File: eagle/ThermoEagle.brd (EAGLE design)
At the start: 100 x 80 mm, 30 parts, among them IC1 MAX232, IC2 4511N, Q1 20MHz, T1 2N2219, T2 2N2219, U1 LM324

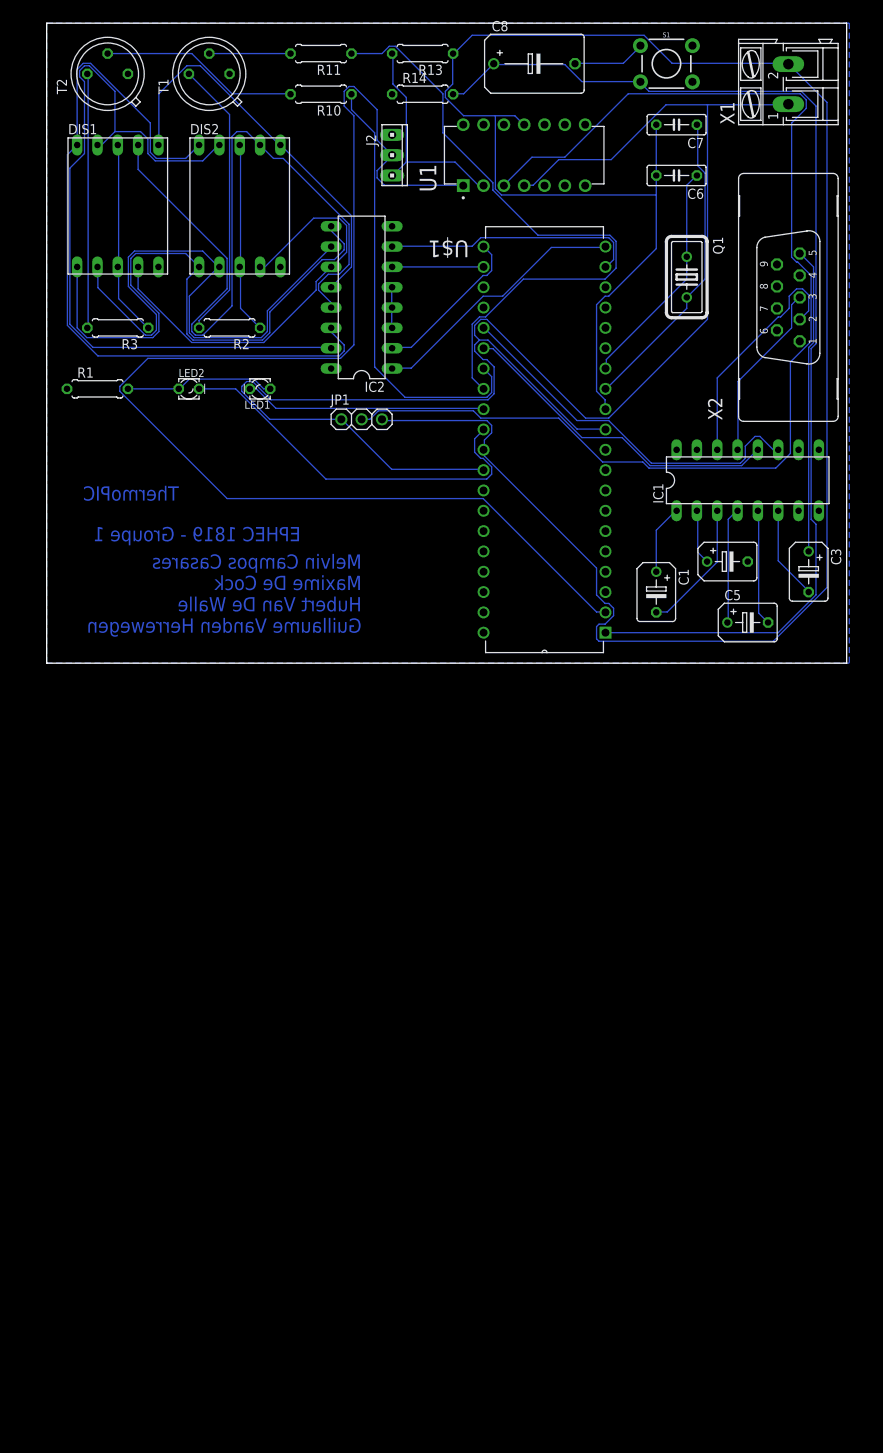
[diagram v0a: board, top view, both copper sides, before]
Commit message: connector
ajout des connecteurs, pour les parties non connectées
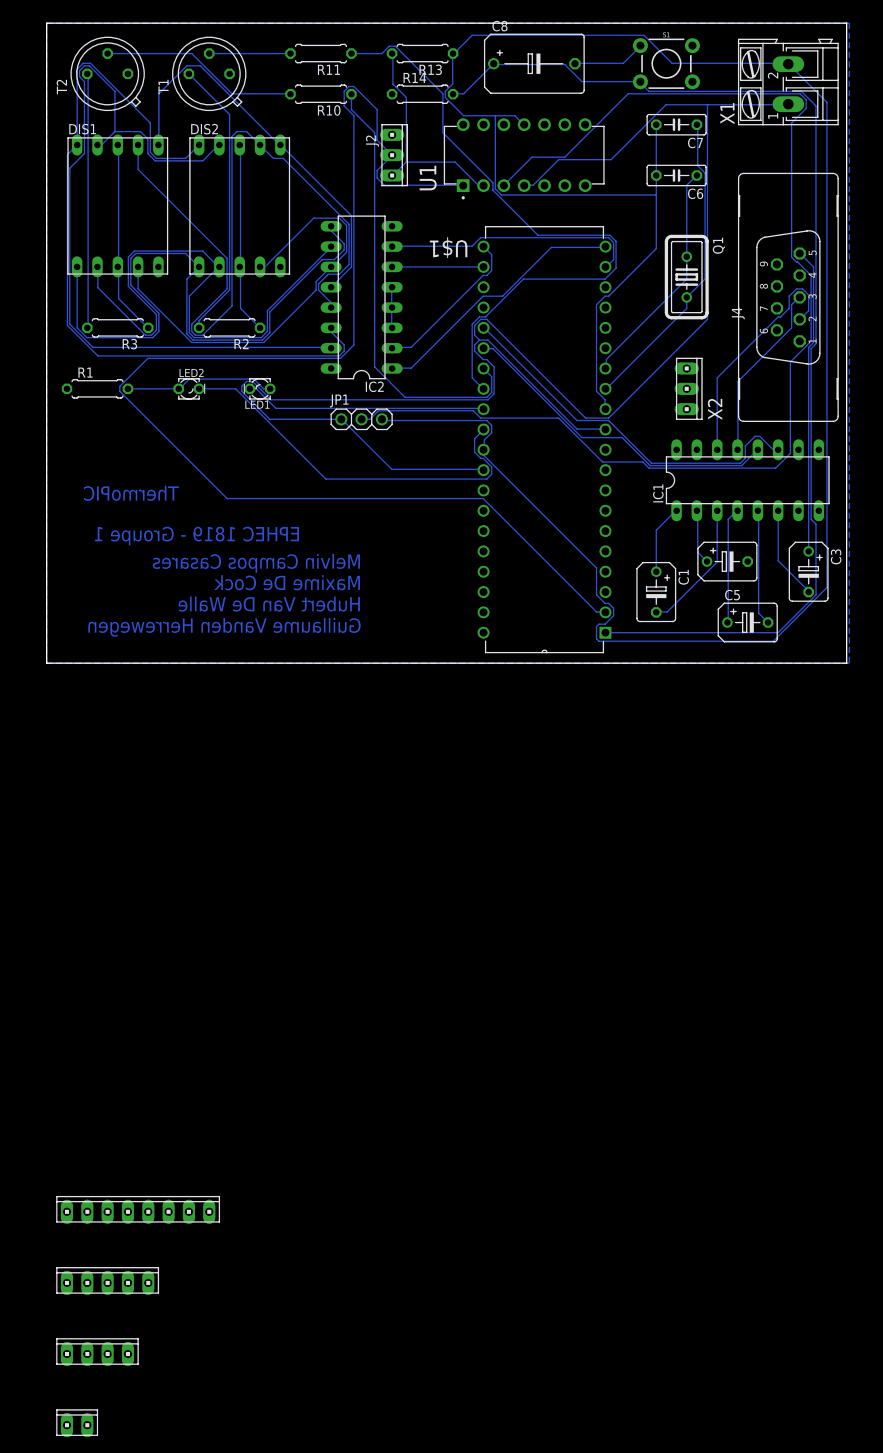
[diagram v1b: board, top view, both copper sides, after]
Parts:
- added J1: (no value), con-amp:10X04MTA
- added J3: (no value), con-amp:10X02MTA
- added J4: (no value), con-amp:10X03MTA
- added J7: (no value), con-amp:10X08MTA
- added J8: (no value), con-amp:10X05MTA
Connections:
- new net N$32: J8.5, U$1.3
- new net N$33: J8.4, U$1.4
- new net N$34: J8.3, U$1.5
- new net N$35: J8.2, U$1.6
- new net N$47: J8.1, U$1.7
- new net N$50: J7.8, U$1.33
- new net N$51: J7.7, U$1.34
- new net N$54: J7.6, U$1.35
- new net N$58: J7.5, U$1.36
- new net N$59: J7.4, U$1.37
- new net N$60: J7.3, U$1.38
- new net N$61: J7.2, U$1.39
- new net N$62: J7.1, U$1.40
- new net N$63: J4.1, U$1.8
- new net N$64: J4.2, U$1.9
- new net N$65: J4.3, U$1.10
- new net N$66: J1.1, U$1.15
- new net N$67: J1.2, U$1.16
- new net N$68: J1.3, U$1.17
- new net N$69: J1.4, U$1.18
- new net N$70: J3.1, U$1.23
- new net N$71: J3.2, U$1.24
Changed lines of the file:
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@@
 <?xml version="1.0" encoding="utf-8"?>
 <!DOCTYPE eagle SYSTEM "eagle.dtd">
-<eagle version="9.3.1">
+<eagle version="9.3.0">
 <drawing>
 <settings>
@@
 <attribute name="VALUE" x="11.176" y="42.4688" size="1.27" layer="27" ratio="10" rot="R180"/>
 </element>
+<element name="J4" library="con-amp" library_urn="urn:adsk.eagle:library:127" package="10X03MTA" package3d_urn="urn:adsk.eagle:package:8081621/1" value="" x="80.01" y="34.29" smashed="yes" rot="R270">
+<attribute name="NAME" x="85.6488" y="44.5262" size="1.27" layer="25" rot="R270"/>
+<attribute name="VALUE" x="82.1609" y="38.0662" size="1.27" layer="27" rot="R270"/>
+</element>
+<element name="J7" library="con-amp" library_urn="urn:adsk.eagle:library:127" package="10X08MTA" value="" x="11.43" y="-68.58" smashed="yes">
+<attribute name="VALUE" x="1.3538" y="-66.3293" size="1.27" layer="27"/>
+</element>
+<element name="J8" library="con-amp" library_urn="urn:adsk.eagle:library:127" package="10X05MTA" value="" x="7.62" y="-77.47" smashed="yes">
+<attribute name="VALUE" x="1.4437" y="-75.3191" size="1.27" layer="27"/>
+</element>
+<element name="J1" library="con-amp" library_urn="urn:adsk.eagle:library:127" package="10X04MTA" value="" x="6.35" y="-86.36" smashed="yes">
+<attribute name="VALUE" x="1.3739" y="-84.2091" size="1.27" layer="27"/>
+</element>
+<element name="J3" library="con-amp" library_urn="urn:adsk.eagle:library:127" package="10X02MTA" value="" x="3.81" y="-95.25" smashed="yes">
+<attribute name="VALUE" x="1.2639" y="-93.0991" size="1.27" layer="27"/>
+</element>
 </elements>
 <signals>
@@
 <wire x1="54.5592" y1="59.7408" x2="54.61" y2="59.69" width="0.1524" layer="16"/>
 </signal>
+<signal name="N$32">
+<contactref element="U$1" pad="3"/>
+<contactref element="J8" pad="5"/>
+<wire x1="2.54" y1="-77.47" x2="69.85" y2="8.89" width="0" layer="19" extent="1-1"/>
+</signal>
+<signal name="N$33">
+<contactref element="U$1" pad="4"/>
+<contactref element="J8" pad="4"/>
+<wire x1="5.08" y1="-77.47" x2="69.85" y2="11.43" width="0" layer="19" extent="1-1"/>
+</signal>
+<signal name="N$34">
+<contactref element="U$1" pad="5"/>
+<contactref element="J8" pad="3"/>
+<wire x1="7.62" y1="-77.47" x2="69.85" y2="13.97" width="0" layer="19" extent="1-1"/>
+</signal>
+<signal name="N$35">
+<contactref element="U$1" pad="6"/>
+<contactref element="J8" pad="2"/>
+<wire x1="10.16" y1="-77.47" x2="69.85" y2="16.51" width="0" layer="19" extent="1-1"/>
+</signal>
+<signal name="N$47">
+<contactref element="U$1" pad="7"/>
+<contactref element="J8" pad="1"/>
+<wire x1="12.7" y1="-77.47" x2="69.85" y2="19.05" width="0" layer="19" extent="1-1"/>
+</signal>
+<signal name="N$50">
+<contactref element="U$1" pad="33"/>
+<contactref element="J7" pad="8"/>
+<wire x1="2.54" y1="-68.58" x2="54.61" y2="21.59" width="0" layer="19" extent="1-1"/>
+</signal>
+<signal name="N$51">
+<contactref element="U$1" pad="34"/>
+<contactref element="J7" pad="7"/>
+<wire x1="5.08" y1="-68.58" x2="54.61" y2="19.05" width="0" layer="19" extent="1-1"/>
+</signal>
+<signal name="N$54">
+<contactref element="U$1" pad="35"/>
+<contactref element="J7" pad="6"/>
+<wire x1="7.62" y1="-68.58" x2="54.61" y2="16.51" width="0" layer="19" extent="1-1"/>
+</signal>
+<signal name="N$58">
+<contactref element="U$1" pad="36"/>
+<contactref element="J7" pad="5"/>
+<wire x1="10.16" y1="-68.58" x2="54.61" y2="13.97" width="0" layer="19" extent="1-1"/>
+</signal>
+<signal name="N$59">
+<contactref element="U$1" pad="37"/>
+<contactref element="J7" pad="4"/>
+<wire x1="12.7" y1="-68.58" x2="54.61" y2="11.43" width="0" layer="19" extent="1-1"/>
+</signal>
+<signal name="N$60">
+<contactref element="U$1" pad="38"/>
+<contactref element="J7" pad="3"/>
+<wire x1="15.24" y1="-68.58" x2="54.61" y2="8.89" width="0" layer="19" extent="1-1"/>
+</signal>
+<signal name="N$61">
+<contactref element="U$1" pad="39"/>
+<contactref element="J7" pad="2"/>
+<wire x1="17.78" y1="-68.58" x2="54.61" y2="6.35" width="0" layer="19" extent="1-1"/>
+</signal>
+<signal name="N$62">
+<contactref element="U$1" pad="40"/>
+<contactref element="J7" pad="1"/>
+<wire x1="20.32" y1="-68.58" x2="54.61" y2="3.81" width="0" layer="19" extent="1-1"/>
+</signal>
+<signal name="N$63">
+<contactref element="J4" pad="1"/>
+<contactref element="U$1" pad="8"/>
+<wire x1="80.01" y1="31.75" x2="69.85" y2="21.59" width="0" layer="19" extent="1-1"/>
+</signal>
+<signal name="N$64">
+<contactref element="J4" pad="2"/>
+<contactref element="U$1" pad="9"/>
+<wire x1="80.01" y1="34.29" x2="69.85" y2="24.13" width="0" layer="19" extent="1-1"/>
+</signal>
+<signal name="N$65">
+<contactref element="J4" pad="3"/>
+<contactref element="U$1" pad="10"/>
+<wire x1="80.01" y1="36.83" x2="69.85" y2="26.67" width="0" layer="19" extent="1-1"/>
+</signal>
+<signal name="N$66">
+<contactref element="U$1" pad="15"/>
+<contactref element="J1" pad="1"/>
+<wire x1="10.16" y1="-86.36" x2="69.85" y2="39.37" width="0" layer="19" extent="1-1"/>
+</signal>
+<signal name="N$67">
+<contactref element="U$1" pad="16"/>
+<contactref element="J1" pad="2"/>
+<wire x1="7.62" y1="-86.36" x2="69.85" y2="41.91" width="0" layer="19" extent="1-1"/>
+</signal>
+<signal name="N$68">
+<contactref element="U$1" pad="17"/>
+<contactref element="J1" pad="3"/>
+<wire x1="5.08" y1="-86.36" x2="69.85" y2="44.45" width="0" layer="19" extent="1-1"/>
+</signal>
+<signal name="N$69">
+<contactref element="U$1" pad="18"/>
+<contactref element="J1" pad="4"/>
+<wire x1="2.54" y1="-86.36" x2="69.85" y2="46.99" width="0" layer="19" extent="1-1"/>
+</signal>
+<signal name="N$70">
+<contactref element="U$1" pad="23"/>
+<contactref element="J3" pad="1"/>
+<wire x1="5.08" y1="-95.25" x2="54.61" y2="46.99" width="0" layer="19" extent="1-1"/>
+</signal>
+<signal name="N$71">
+<contactref element="U$1" pad="24"/>
+<contactref element="J3" pad="2"/>
+<wire x1="2.54" y1="-95.25" x2="54.61" y2="44.45" width="0" layer="19" extent="1-1"/>
+</signal>
 </signals>

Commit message: Final update ThermoEagle board
With connectors for parts that aren't connected + isolation
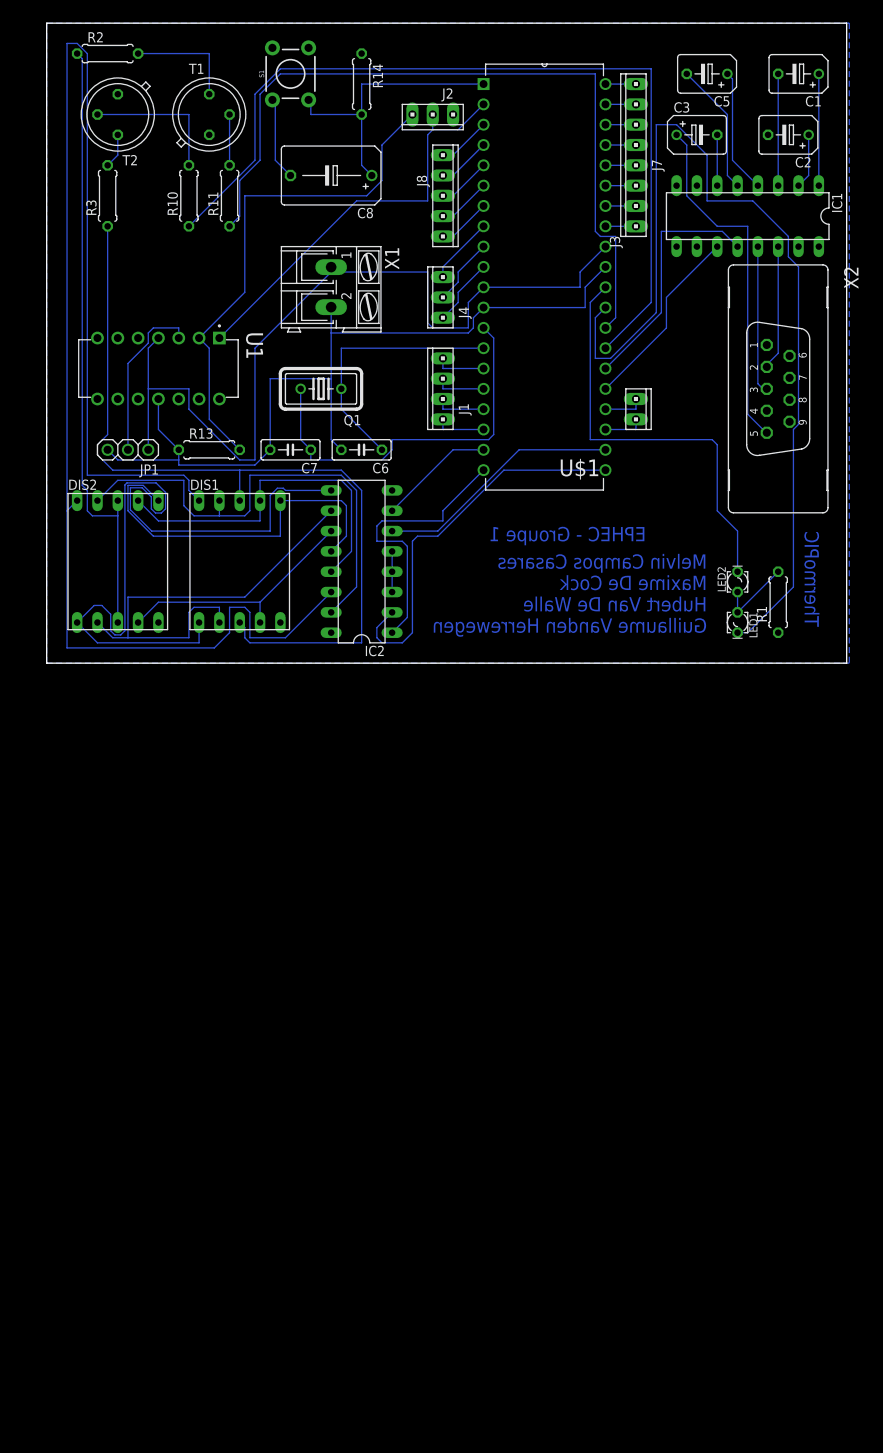
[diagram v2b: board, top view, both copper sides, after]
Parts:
- moved J7 146.0 mm to (73.7, 63.5), turned to 90 degrees
- moved J3 144.9 mm to (73.7, 31.8), turned to 270 degrees
- moved J8 142.2 mm to (49.5, 58.4), turned to 270 degrees
- moved J1 128.1 mm to (49.5, 34.3), turned to 90 degrees
- moved R1 89.2 mm to (91.4, 7.62), turned to 90 degrees
- moved LED2 72.7 mm to (86.4, 10.2), turned to 90 degrees
- moved C5 68.8 mm to (82.5, 73.7), turned to 180 degrees
- moved C1 67.2 mm to (94.0, 73.7), turned to 180 degrees
- moved LED1 66.5 mm to (86.4, 5.08), turned to 270 degrees
- moved C7 63.1 mm to (30.5, 26.7)
- moved X1 62.5 mm to (35.6, 47.0), turned to 270 degrees
- moved C3 56.4 mm to (81.3, 66.0), turned to 0 degrees
- moved R13 56.3 mm to (20.3, 26.7), turned to 0 degrees
- moved C2 53.9 mm to (92.7, 66.0), turned to 180 degrees
- moved U1 52.9 mm to (14.0, 36.8), turned to 270 degrees
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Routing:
- net GND: track 279.1 -> 105.8 mm
- net N$48: track 147.8 -> 21.0 mm
- net N$49: track 163.2 -> 51.9 mm
- net N$55: track 139.1 -> 35.4 mm
- net N$36: track 95.9 -> 192.0 mm
- net VCC: track 202.4 -> 109.1 mm
- net N$45: track 30.3 -> 120.0 mm
- net N$7: track 24.6 -> 103.9 mm
- net N$12: track 24.1 -> 77.0 mm
- net N$38: track 55.2 -> 108.1 mm
- net N$28: track 90.8 -> 44.5 mm
- net N$31: track 27.7 -> 64.0 mm
- net N$10: track 97.0 -> 61.1 mm
- net N$11: track 19.9 -> 48.4 mm
- net N$30: track 31.9 -> 4.34 mm
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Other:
- board text added: "EPHEC - Groupe 1"
- board text removed: "EPHEC 1819 - Groupe 1"

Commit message: Erreur corrigé
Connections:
- removed net N$5: IC2.3, IC2.4, IC2.5
- new net N$55: IC2.5
- new net N$73: IC2.3, IC2.4
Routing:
- net N$5: track 5.08 -> 0.00 mm
- net N$72: track 35.4 -> 36.4 mm
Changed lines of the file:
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@@
 <?xml version="1.0" encoding="utf-8"?>
 <!DOCTYPE eagle SYSTEM "eagle.dtd">
-<eagle version="9.3.1">
+<eagle version="9.3.0">
 <drawing>
 <settings>
@@
 </polygon>
 </signal>
-<signal name="N$55">
-<contactref element="U$1" pad="1"/>
-<contactref element="C8" pad="+"/>
-<contactref element="S1" pad="3"/>
-<contactref element="R14" pad="2"/>
-<wire x1="33.02" y1="68.58" x2="39.37" y2="68.58" width="0.1524" layer="16"/>
-<wire x1="33.02" y1="69.85" x2="33.02" y2="68.58" width="0.1524" layer="16"/>
-<wire x1="33.02" y1="69.85" x2="32.7406" y2="70.4088" width="0.1524" layer="16"/>
-<wire x1="39.37" y1="62.23" x2="40.64" y2="60.96" width="0.1524" layer="16"/>
-<wire x1="39.37" y1="68.58" x2="39.37" y2="62.23" width="0.1524" layer="16"/>
-<wire x1="39.37" y1="72.39" x2="54.61" y2="72.39" width="0.1524" layer="16"/>
-<wire x1="39.37" y1="68.58" x2="39.37" y2="72.39" width="0.1524" layer="16"/>
-</signal>
 <signal name="N$56">
 <contactref element="S1" pad="1"/>
@@
 <contactref element="R11" pad="2"/>
 <wire x1="22.86" y1="68.58" x2="22.86" y2="62.23" width="0.1524" layer="16"/>
-</signal>
-<signal name="N$5">
-<contactref element="IC2" pad="3"/>
-<contactref element="IC2" pad="4"/>
-<contactref element="IC2" pad="5"/>
-<wire x1="43.18" y1="11.43" x2="43.18" y2="8.89" width="0.1524" layer="16"/>
-<wire x1="43.18" y1="11.43" x2="43.18" y2="13.97" width="0.1524" layer="16"/>
 </signal>
 <signal name="N$23">
@@
 <wire x1="73.66" y1="33.02" x2="73.66" y2="31.75" width="0.1524" layer="16"/>
 </signal>
+<signal name="N$72">
+<contactref element="U$1" pad="1"/>
+<contactref element="C8" pad="+"/>
+<contactref element="S1" pad="3"/>
+<contactref element="R14" pad="2"/>
+<wire x1="39.37" y1="68.58" x2="45.847" y2="75.057" width="0.1524" layer="16"/>
+<wire x1="39.37" y1="62.23" x2="40.64" y2="60.96" width="0.1524" layer="16"/>
+<wire x1="39.37" y1="68.58" x2="39.37" y2="62.23" width="0.1524" layer="16"/>
+<wire x1="39.37" y1="72.39" x2="54.61" y2="72.39" width="0.1524" layer="16"/>
+<wire x1="39.37" y1="68.58" x2="39.37" y2="72.39" width="0.1524" layer="16"/>
+<wire x1="39.37" y1="68.58" x2="32.7406" y2="70.4088" width="0" layer="19" extent="1-1"/>
+</signal>
+<signal name="N$55">
+<contactref element="IC2" pad="5"/>
+</signal>
+<signal name="N$73">
+<contactref element="IC2" pad="4"/>
+<contactref element="IC2" pad="3"/>
+<wire x1="43.18" y1="8.89" x2="43.18" y2="11.43" width="0" layer="19" extent="1-1"/>
+</signal>
 </signals>

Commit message: Update ThermoEagle board
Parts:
- moved R2 17.8 mm to (7.62, 58.4), turned to 90 degrees
- moved J4 5.24 mm to (48.3, 50.8), turned to 180 degrees
- moved R3 5.08 mm to (12.7, 58.4)
- moved JP1 5.08 mm to (10.2, 31.8)
- moved R13 5.08 mm to (20.3, 31.8)
- moved U1 3.81 mm to (14.0, 40.6)
- moved J8 2.84 mm to (50.8, 61.0)
- moved J2 2.54 mm to (48.3, 71.1)
- moved Q1 1.80 mm to (35.6, 35.6)
- moved C6 1.80 mm to (40.6, 27.9)
- moved DIS2 1.80 mm to (10.2, 14.0)
- moved C7 1.80 mm to (31.8, 27.9)
- moved J1 1.80 mm to (50.8, 33.0)
- moved C8 1.27 mm to (34.3, 61.0)
- moved X1 1.27 mm to (34.3, 47.0)
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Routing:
- net N$36: track 192.0 -> 32.6 mm
- net N$45: track 120.0 -> 53.8 mm
- net N$26: track 31.4 -> 72.1 mm
- net N$11: track 48.4 -> 80.0 mm
- net N$24: track 95.3 -> 71.1 mm
- net N$7: track 103.9 -> 127.4 mm
- net N$10: track 61.1 -> 82.4 mm
- net N$12: track 77.0 -> 96.6 mm
- net VCC: track 109.1 -> 95.4 mm
- net N$28: track 44.5 -> 31.4 mm
- net N$9: track 14.0 -> 25.5 mm
- net N$6: track 34.5 -> 25.8 mm
- net N$27: track 47.6 -> 39.4 mm
- net RX: track 30.4 -> 22.8 mm
- net GND: track 105.8 -> 112.1 mm
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
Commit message: Update ThermoEagle board #IamBRD
Once more updated but still needs further improvements I think...
Maxime needs to perform a complete analysis if because there are lots of
things not connected to GND or VCC !
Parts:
- moved X1 34.1 mm to (10.2, 71.1)
- moved R2 23.3 mm to (27.9, 47.0)
- moved R3 22.2 mm to (31.8, 47.0)
- moved R10 21.1 mm to (35.6, 47.0)
- moved R11 20.1 mm to (39.4, 47.0)
- moved T1 10.2 mm to (19.1, 58.4)
- moved T2 10.2 mm to (8.89, 58.4)
- moved LED2 2.54 mm to (87.6, 12.7)
- moved IC2 1.27 mm to (39.4, 14.0)
- moved R1 1.27 mm to (91.4, 8.89)
- moved LED1 1.27 mm to (87.6, 6.35)
- moved S1 1.27 mm to (30.5, 72.4)
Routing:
- net N$49: track 51.4 -> 151.0 mm
- net N$31: track 61.4 -> 143.5 mm
- net N$30: track 5.39 -> 54.4 mm
- net N$4: track 17.8 -> 66.6 mm
- net N$44: track 96.8 -> 51.4 mm
- net N$38: track 108.1 -> 63.8 mm
- net N$11: track 80.0 -> 38.9 mm
- net GND: track 112.1 -> 150.1 mm
- net N$26: track 72.1 -> 41.8 mm
- net N$7: track 127.4 -> 97.2 mm
- net N$12: track 96.6 -> 69.2 mm
- net VCC: track 95.4 -> 76.4 mm
- net N$3: track 6.35 -> 25.2 mm
- net N$36: track 32.6 -> 49.8 mm
- net N$53: track 47.8 -> 36.0 mm
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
